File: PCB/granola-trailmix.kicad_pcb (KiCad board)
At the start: 2 copper layers, 210.1 x 98.3 mm, 46 parts, among them J1 Conn_01x02, J2 USB_B_Micro, SW1 6mm_Button, SW10 MX_Switch, SW11 MX_Switch, SW12 MX_Switch, SW13 MX_Switch, SW14 MX_Switch, SW15 MX_Switch, SW16 MX_Switch, SW17 MX_Switch, SW18 MX_Switch, SW2 6mm_Button, SW3 6mm_Button, SW4 6mm_Button, SW5 6mm_Button, SW6 6mm_Button, SW7 MX_Switch, SW8 MX_Switch, SW9 MX_Switch, U1 AMS1117-3.3_SOT223, U2 W25Q128JVS, U3 RP2040, Y1 ABLS-12.000MHZ-B4-T

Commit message: usb-c
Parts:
- removed J2: USB_B_Micro, Connector_USB:USB_Micro-B_Amphenol_10103594-0001LF_Horizontal
- added R6: 5.1k, Resistor_SMD:R_0402_1005Metric, F.Cu at (130.0, 44.4)
- added R7: 5.1k, Resistor_SMD:R_0402_1005Metric, F.Cu at (137.9, 45.3)
- added USB1: HRO-TYPE-C-31-M-12, Type-C:HRO-TYPE-C-31-M-12-Assembly, F.Cu at (136.5, 35.2)
- moved C1 9.80 mm to (140.6, 45.6), turned to 0 degrees
- moved SW15 5.59 mm to (153.7, 100.1)
- moved SW16 5.59 mm to (181.6, 88.1)
- moved SW17 5.59 mm to (209.8, 92.5)
- moved SW11 5.59 mm to (157.1, 70.3)
- moved SW12 5.59 mm to (185.2, 58.4)
- moved SW13 5.59 mm to (213.1, 63.0)
- moved SW14 5.59 mm to (241.3, 74.8)
- moved SW18 5.59 mm to (237.7, 104.6)
- moved U1 5.42 mm to (136.2, 52.6), turned to 180 degrees
- moved C2 2.62 mm to (134.1, 47.3), turned to 0 degrees
- moved SW8 2.03 mm to (89.9, 58.2)
- moved R3 1.77 mm to (127.0, 44.7), turned to 180 degrees
- moved R4 1.21 mm to (127.0, 46.0), turned to 180 degrees
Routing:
- net GND: track 893.1 -> 922.6 mm
- net +3V3: track 108.8 -> 93.3 mm
- net /USB_D+: track 3.82 -> 14.3 mm
- net /USB_D-: track 3.85 -> 14.2 mm
- net /2K: track 89.6 -> 95.3 mm
- net /1P: track 65.0 -> 70.7 mm
- net /1K: track 72.0 -> 77.5 mm
- net Net-(R6-Pad1): track 0.00 -> 5.33 mm
- net /3K: track 117.5 -> 121.5 mm
- net /4K: track 157.1 -> 159.2 mm
- net /DOWN: track 35.8 -> 33.8 mm
- net Net-(R7-Pad1): track 0.00 -> 1.97 mm
- net /3P: track 132.4 -> 134.3 mm
- net /S2: track 120.7 -> 119.0 mm
- net /4P: track 154.0 -> 155.7 mm
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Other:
- board text added: "Granola Arcade: https://granola.games/ Usage Guide: https://gp2040-ce.info/"
- board text removed: "Board Design by Michael Switzer Usage Guide: https://gp2040-ce.info/"

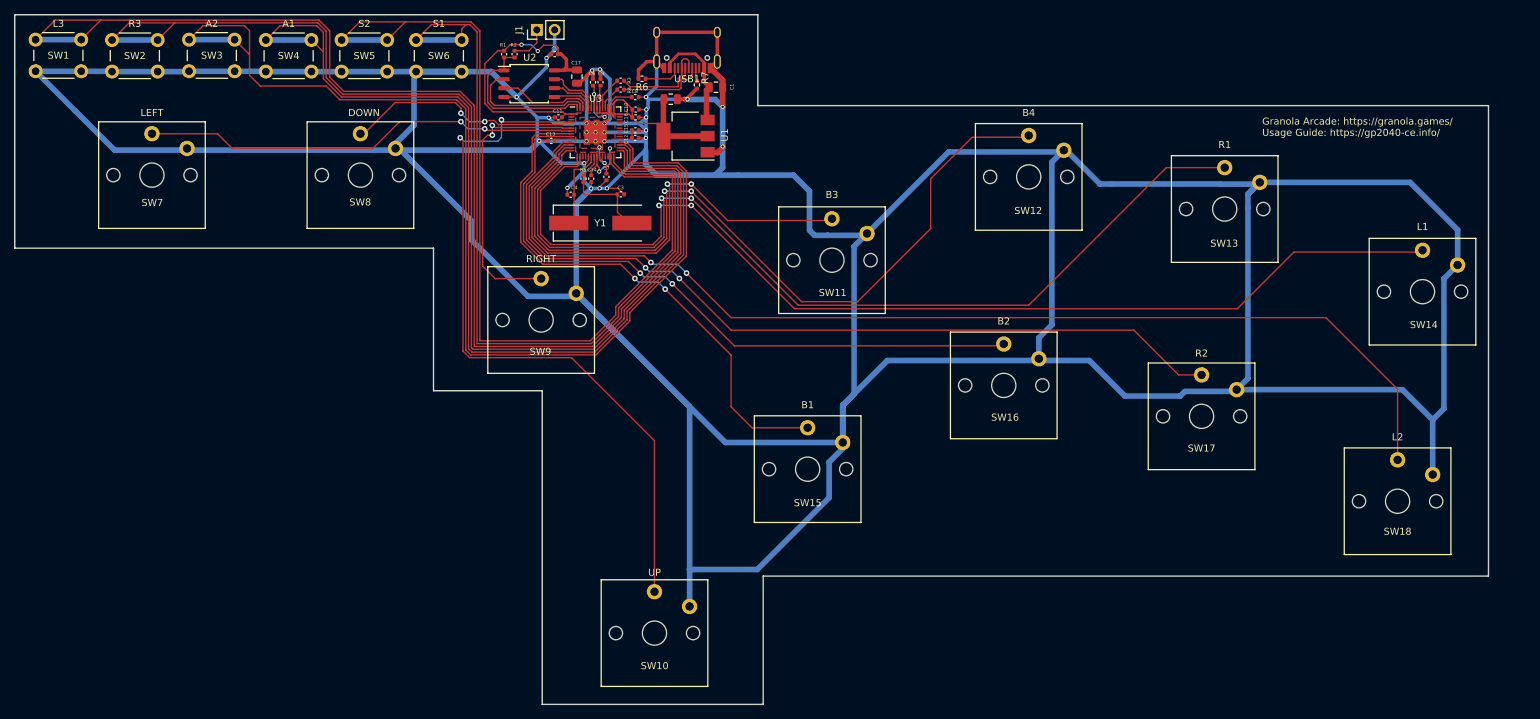
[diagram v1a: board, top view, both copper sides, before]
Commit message: vertical print case, minor pcb changes
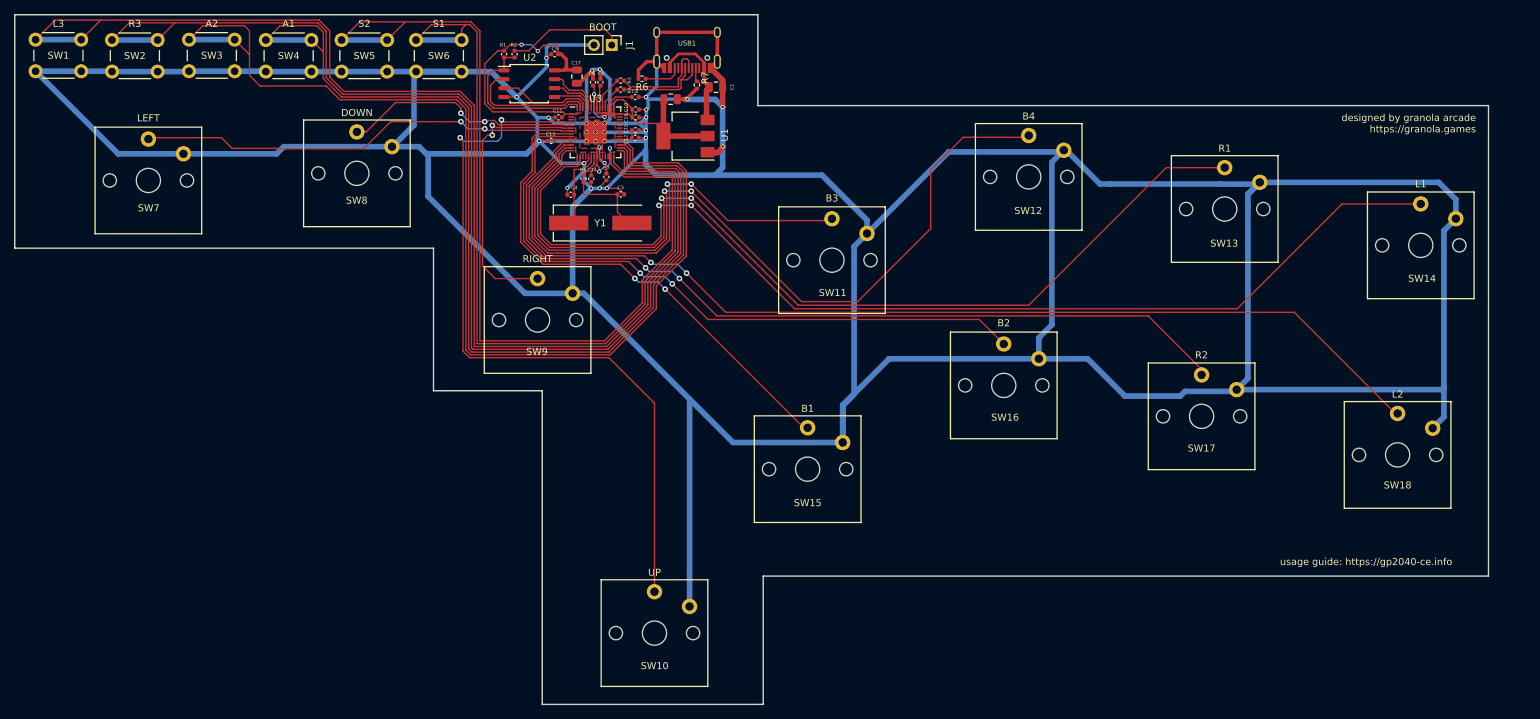
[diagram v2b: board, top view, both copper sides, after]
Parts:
- moved J1 10.9 mm to (125.7, 39.6), turned to -90 degrees
- moved SW14 6.61 mm to (241.0, 68.2)
- moved SW18 6.60 mm to (237.7, 98.0)
- moved SW7 0.92 mm to (59.7, 58.9)
- moved SW8 0.57 mm to (89.4, 57.9)
- moved SW9 0.51 mm to (115.2, 78.8)
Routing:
- net GND: track 922.6 -> 863.7 mm
- net /~{USB_BOOT}: track 5.48 -> 16.7 mm
- net /4K: track 159.2 -> 150.5 mm
- net /1K: track 77.5 -> 73.2 mm
- net /UP: track 103.7 -> 106.8 mm
- net /4P: track 155.7 -> 158.1 mm
- net /S2: track 119.0 -> 120.2 mm
- net /L3: track 174.9 -> 176.1 mm
- net /R3: track 164.7 -> 165.9 mm
- net /S1: track 130.2 -> 131.4 mm
- net /A2: track 155.5 -> 156.7 mm
- net /A1: track 142.8 -> 144.0 mm
- net /2P: track 114.6 -> 115.3 mm
- net /RIGHT: track 41.5 -> 41.0 mm
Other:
- board text added: "BOOT"
- board text added: "designed by granola arcade https://granola.games"
- board text added: "usage guide: https://gp2040-ce.info"
- board text removed: "Granola Arcade: https://granola.games/ Usage Guide: https://gp2040-ce.info/"

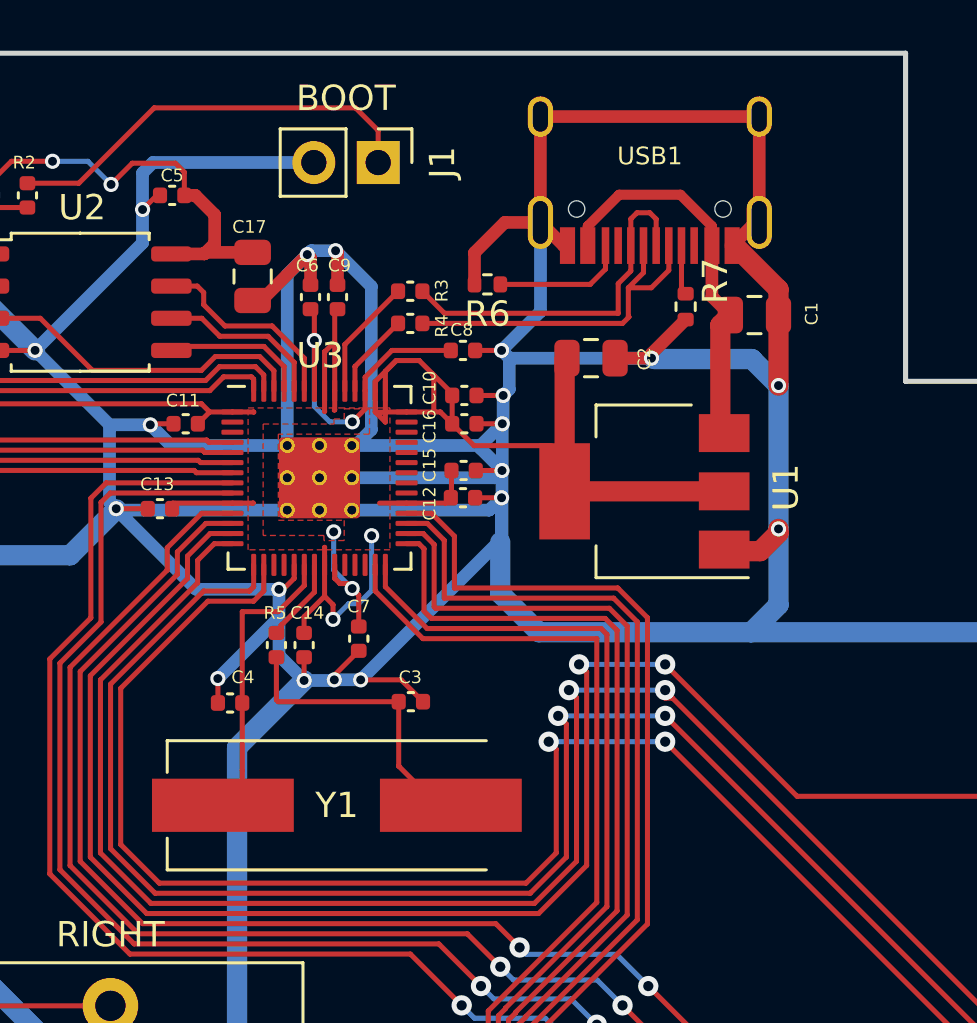
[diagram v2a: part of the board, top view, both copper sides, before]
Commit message: Updated PCB to new crystal. Added version of TrailMix case that has no front design.
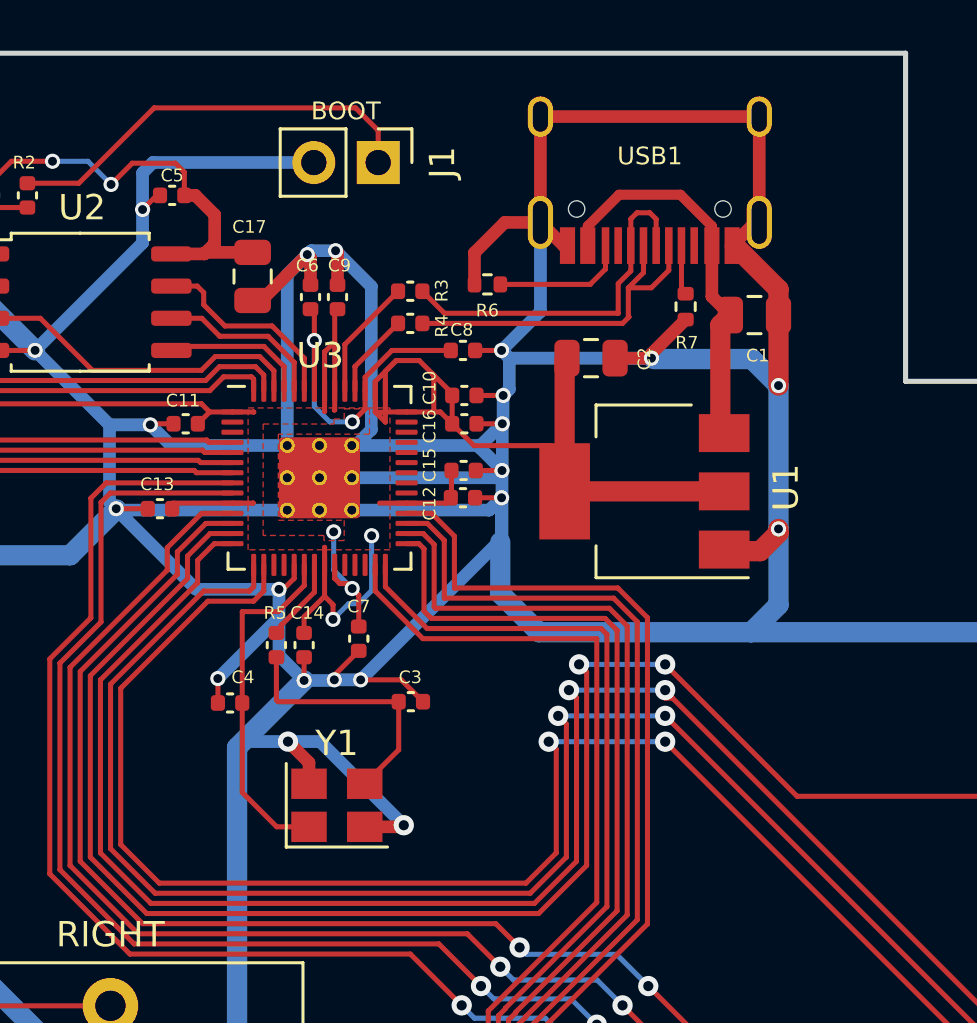
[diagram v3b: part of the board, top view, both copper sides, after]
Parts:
- Y1: footprint RP2040_minimal:Crystal_SMD_HC49-US -> Crystal:Crystal_SMD_3225-4Pin_3.2x2.5mm
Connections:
- Y1 pad 2: Net-(C3-Pad1) -> GND
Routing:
- net GND: track 863.7 -> 875.3 mm, vias 19 -> 21
- net /XIN: track 11.7 -> 14.0 mm
- net Net-(C3-Pad1): track 11.8 -> 10.3 mm
